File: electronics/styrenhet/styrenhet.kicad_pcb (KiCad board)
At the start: 2 copper layers, 160 x 100 mm, 42 parts, among them J1 12V Fan, J2 Battery_In, J3 Battery to MCU, J4 12V Fan, J5 IDE PATA Connector, U1 motor_driver, U2 motor_driver, U3 motor_driver, U4 motor_driver

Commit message: Strax etss
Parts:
- moved C8 0.60 mm to (169.0, 92.6)
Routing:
- net GND: track 251.5 -> 234.1 mm, vias 7 -> 6
- net /L_EN_4: track 136.4 -> 142.7 mm
- net /L_IS_4: track 165.3 -> 169.9 mm
- net /LPWM_4: track 120.0 -> 123.2 mm
- net /R_IS_4: track 129.6 -> 132.6 mm
- net /L_IS_2: track 57.6 -> 60.1 mm
- net /R_EN_4: track 113.6 -> 115.9 mm
- net /RPWM_4: track 99.5 -> 101.6 mm
- net /L_EN_1: track 99.5 -> 98.1 mm
- net /L_EN_2: track 45.5 -> 46.8 mm
- net /LPWM_1: track 102.4 -> 103.7 mm
- net /LPWM_2: track 20.4 -> 21.0 mm
- net /R_IS_3: track 148.2 -> 147.7 mm
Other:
- net class Default: clearance 0.2 -> 0.3
- rule trace_clearance: 0.2 -> 0.3

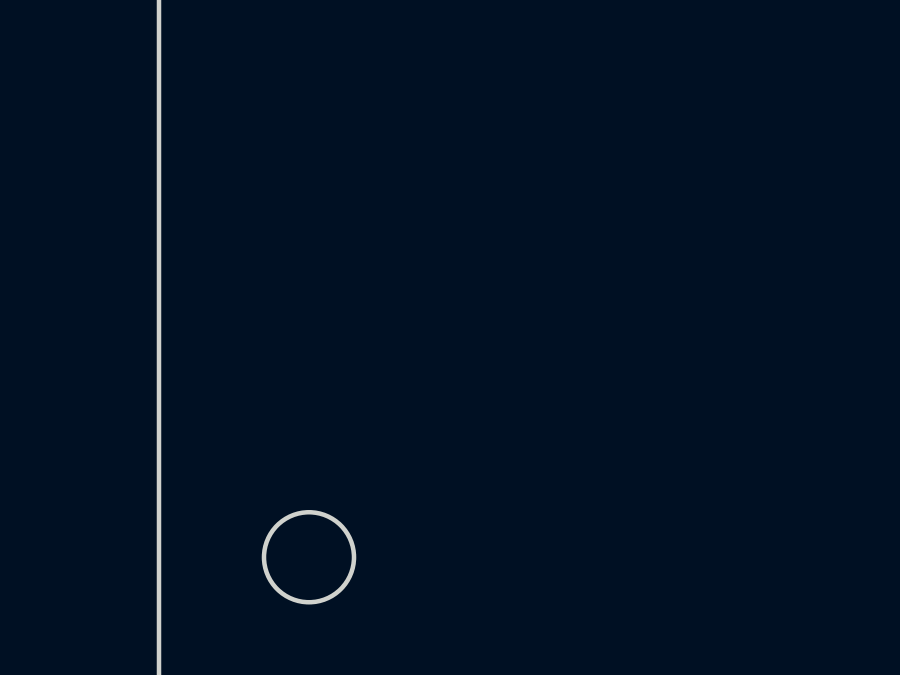
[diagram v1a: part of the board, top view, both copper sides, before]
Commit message: Add text to svg
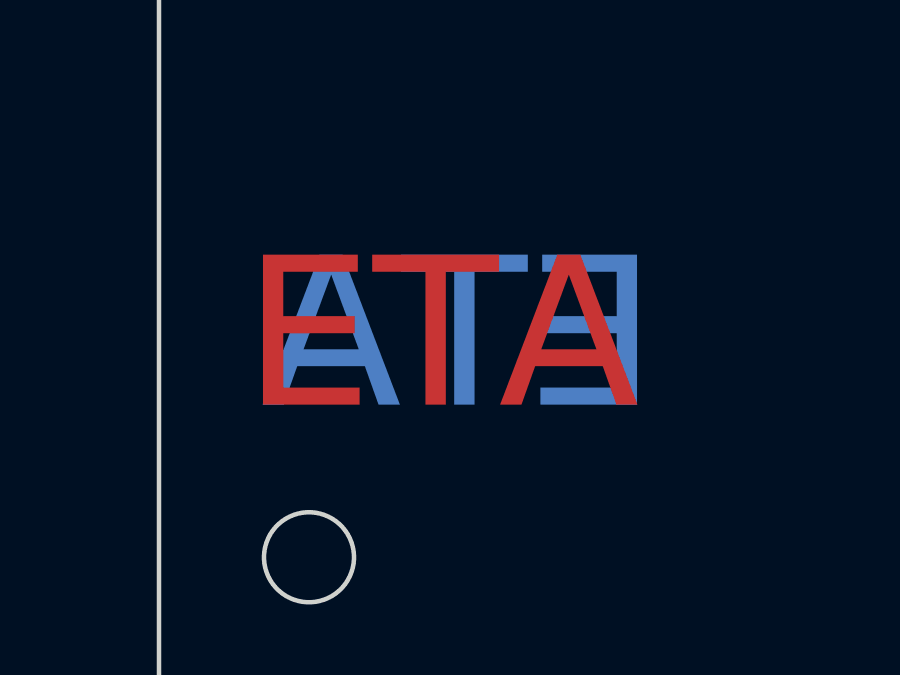
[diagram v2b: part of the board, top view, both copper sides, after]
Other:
- board text added: "ETA"
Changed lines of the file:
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@@
   (general
     (thickness 1.6)
-    (drawings 11)
+    (drawings 13)
     (tracks 535)
     (zones 0)
@@
       (excludeedgelayer true)
       (linewidth 0.100000)
-      (plotframeref false)
+      (plotframeref true)
       (viasonmask false)
       (mode 1)
@@
       (subtractmaskfromsilk false)
       (outputformat 5)
-      (mirror false)
-      (drillshape 2)
+      (mirror true)
+      (drillshape 1)
       (scaleselection 1)
       (outputdirectory ""))
@@
     )
   )
+  (gr_text ETA (at 59.4 137.6) (layer F.Cu)
+    (effects (font (size 5 5) (thickness 0.3)))
+  )
+  (gr_text ETA (at 60 137.6) (layer B.Cu)
+    (effects (font (size 5 5) (thickness 0.3)) (justify mirror))
+  )
   (gr_circle (center 55 55) (end 55 56.5) (layer Edge.Cuts) (width 0.15))

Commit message: ...
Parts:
- removed C19: CP, Capacitors_THT:CP_Radial_D22.0mm_P10.00mm_SnapIn
- C17: moved to B.Cu
- moved C18 11.2 mm to (92.0, 126.0)
- moved C7 9.69 mm to (160.0, 110.4)
- moved C17 6.42 mm to (135.6, 73.6)
- moved C6 5.16 mm to (149.2, 110.4)
- moved C8 4.02 mm to (173.0, 93.0)
- moved C10 1.71 mm to (101.2, 111.2), turned to 0 degrees
- moved R11 1.60 mm to (170.1, 110.7)
- moved R3 1.60 mm to (167.5, 110.7)
- moved C20 1.58 mm to (165.0, 130.0), turned to 0 degrees
- moved C5 1.46 mm to (155.8, 85.2)
- moved C11 0.80 mm to (116.0, 115.8)
- moved R15 0.80 mm to (117.0, 110.2)
- moved R7 0.80 mm to (114.5, 110.2)
- moved C15 0.50 mm to (161.0, 97.0)
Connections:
- J5 pad 10: /L_IS_3 -> /L_IS_4
- J5 pad 11: /LPWM_1 -> /RPWM_1
- J5 pad 13: /R_EN_1 -> /L_EN_1
- J5 pad 16: /R_EN_3 -> /L_EN_3
- J5 pad 18: /LPWM_3 -> /RPWM_3
- J5 pad 19: /L_IS_1 -> /L_IS_2
- J5 pad 20: /RPWM_3 -> /LPWM_3
- J5 pad 21: /RPWM_2 -> /LPWM_2
- J5 pad 22: /L_IS_4 -> /L_IS_3
- J5 pad 23: /LPWM_2 -> /RPWM_2
- J5 pad 25: /R_EN_2 -> /L_EN_2
- J5 pad 28: /R_EN_4 -> /L_EN_4
- J5 pad 30: /LPWM_4 -> /RPWM_4
- J5 pad 31: /L_IS_2 -> /L_IS_1
- J5 pad 32: /RPWM_4 -> /LPWM_4
- J5 pad 9: /RPWM_1 -> /LPWM_1
- U1 pad 3: /R_EN_1 -> /L_EN_1
- U2 pad 3: /R_EN_2 -> /L_EN_2
- U3 pad 3: /R_EN_3 -> /L_EN_3
- U4 pad 3: /R_EN_4 -> /L_EN_4
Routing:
- net /BAT_+: track 84.9 -> 397.8 mm
- net /R_EN_3: track 158.4 -> 0.00 mm
- net /R_EN_4: track 115.9 -> 0.00 mm
- net GND: track 234.1 -> 337.9 mm, vias 6 -> 5
- net /R_EN_1: track 67.9 -> 0.00 mm
- net /L_IS_4: track 169.9 -> 112.8 mm, vias 2 -> 1
- net /L_EN_1: track 98.1 -> 62.7 mm, vias 2 -> 0
- net /R_EN_2: track 32.6 -> 0.00 mm
- net /L_EN_3: track 187.8 -> 158.6 mm, vias 2 -> 0
- net /L_IS_2: track 60.1 -> 32.7 mm, vias 2 -> 0
- net /L_EN_4: track 142.7 -> 122.6 mm, vias 2 -> 0
- net /LPWM_1: track 103.7 -> 86.6 mm, vias 2 -> 0
- net /L_EN_2: track 46.8 -> 33.8 mm, vias 2 -> 0
- net /RPWM_3: track 178.3 -> 166.5 mm
- net /RPWM_2: track 36.2 -> 25.8 mm, vias 2 -> 0
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- added copper zone on F.Cu, net GND
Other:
- net class Default: clearance 0.3 -> 0.5
- rule trace_clearance: 0.3 -> 0.5
